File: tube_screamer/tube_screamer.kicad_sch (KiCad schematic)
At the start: 67 parts, among them J1 Jack_6.35, J2 Jack_6.35, J6 Barrel_Jack_Switch, J7 Conn_01x01_Socket, J8 Conn_01x01_Socket, J9 top_panel_connector, P1 front_plate, P2 bottom_plate, Q1 MMBT5551, Q10 AO3401A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

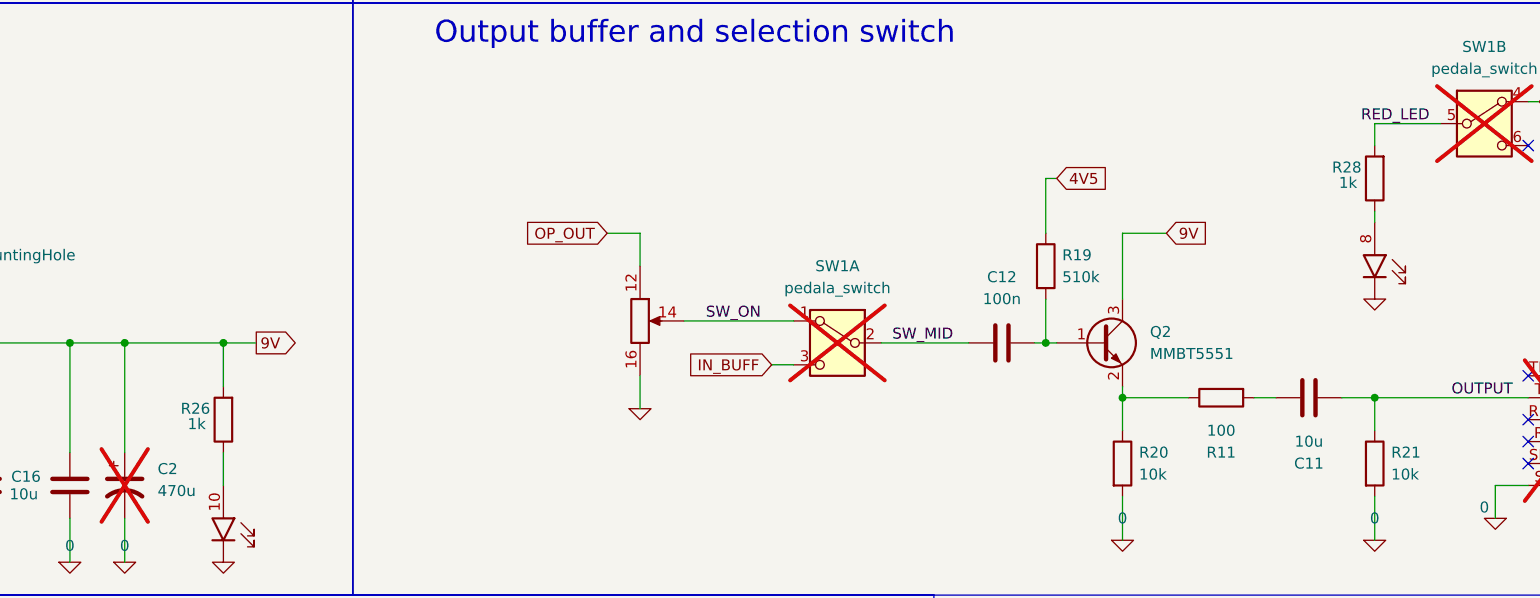
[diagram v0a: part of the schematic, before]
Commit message: 2.2 kOhm LED resistance.
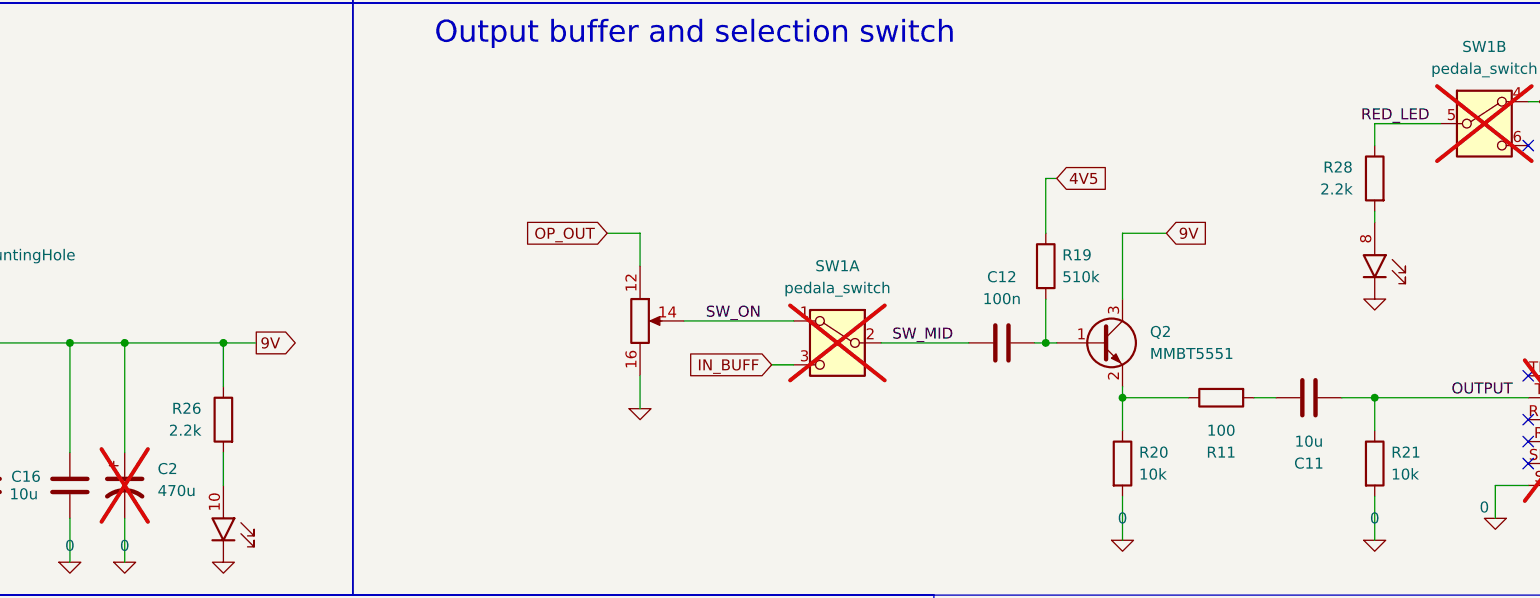
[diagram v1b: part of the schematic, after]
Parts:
- R26, R28: value 1k -> 2.2k; LCSC C21190 -> C4190
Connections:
- net 9V: now also R26.1; no longer R26.2
- net RED_LED: now also R28.1; no longer R28.2
- net at J9.8 (Pin_8): now also R28.2; no longer R28.1
- net at J9.10 (Pin_10): now also R26.2; no longer R26.1
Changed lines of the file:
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@@
 	)
 	(symbol
+		(lib_id "Device:R")
+		(at 93.98 128.27 0)
+		(mirror y)
+		(unit 1)
+		(exclude_from_sim no)
+		(in_bom yes)
+		(on_board yes)
+		(dnp no)
+		(property "Reference" "R26"
+			(at 91.44 126.9999 0)
+			(effects
+				(font
+					(size 1.27 1.27)
+				)
+				(justify left)
+			)
+		)
+		(property "Value" "2.2k"
+			(at 91.44 129.5399 0)
+			(effects
+				(font
+					(size 1.27 1.27)
+				)
+				(justify left)
+			)
+		)
+		(property "Footprint" "Resistor_SMD:R_0603_1608Metric_Pad0.98x0.95mm_HandSolder"
+			(at 95.758 128.27 90)
+			(effects
+				(font
+					(size 1.27 1.27)
+				)
+				(hide yes)
+			)
+		)
+		(property "Datasheet" "~"
+			(at 93.98 128.27 0)
+			(effects
+				(font
+					(size 1.27 1.27)
+				)
+				(hide yes)
+			)
+		)
+		(property "Description" ""
+			(at 93.98 128.27 0)
+			(effects
+				(font
+					(size 1.27 1.27)
+				)
+			)
+		)
+		(property "LCSC" "C4190"
+			(at 93.98 128.27 90)
+			(effects
+				(font
+					(size 1.27 1.27)
+				)
+				(hide yes)
+			)
+		)
+		(pin "1"
+		)
+		(pin "2"
+		)
+		(instances
+			(project "tube_screamer"
+				(path "/e0801131-6974-42d8-8070-4ed960891aa7"
+					(reference "R26")
+					(unit 1)
+				)
+			)
+		)
+	)
+	(symbol
 		(lib_id "pedale:top_panel_connector")
 		(at 181.61 163.83 0)
@@
 	)
 	(symbol
-		(lib_id "Device:R")
-		(at 227.33 100.33 180)
-		(unit 1)
-		(exclude_from_sim no)
-		(in_bom yes)
-		(on_board yes)
-		(dnp no)
-		(property "Reference" "R28"
-			(at 225.806 99.06 0)
-			(effects
-				(font
-					(size 1.27 1.27)
-				)
-				(justify left)
-			)
-		)
-		(property "Value" "1k"
-			(at 225.298 100.838 0)
-			(effects
-				(font
-					(size 1.27 1.27)
-				)
-				(justify left)
-			)
-		)
-		(property "Footprint" "Resistor_SMD:R_0603_1608Metric_Pad0.98x0.95mm_HandSolder"
-			(at 229.108 100.33 90)
-			(effects
-				(font
-					(size 1.27 1.27)
-				)
-				(hide yes)
-			)
-		)
-		(property "Datasheet" "~"
-			(at 227.33 100.33 0)
-			(effects
-				(font
-					(size 1.27 1.27)
-				)
-				(hide yes)
-			)
-		)
-		(property "Description" ""
-			(at 227.33 100.33 0)
-			(effects
-				(font
-					(size 1.27 1.27)
-				)
-			)
-		)
-		(property "LCSC" "C21190"
-			(at 227.33 100.33 90)
-			(effects
-				(font
-					(size 1.27 1.27)
-				)
-				(hide yes)
-			)
-		)
-		(pin "1"
-		)
-		(pin "2"
-		)
-		(instances
-			(project "tube_screamer"
-				(path "/e0801131-6974-42d8-8070-4ed960891aa7"
-					(reference "R28")
-					(unit 1)
-				)
-			)
-		)
-	)
-	(symbol
 		(lib_name "0_10")
 		(lib_id "Simulation_SPICE:0")
@@
 	)
 	(symbol
+		(lib_id "Device:R")
+		(at 227.33 100.33 0)
+		(mirror y)
+		(unit 1)
+		(exclude_from_sim no)
+		(in_bom yes)
+		(on_board yes)
+		(dnp no)
+		(property "Reference" "R28"
+			(at 224.79 99.0599 0)
+			(effects
+				(font
+					(size 1.27 1.27)
+				)
+				(justify left)
+			)
+		)
+		(property "Value" "2.2k"
+			(at 224.79 101.5999 0)
+			(effects
+				(font
+					(size 1.27 1.27)
+				)
+				(justify left)
+			)
+		)
+		(property "Footprint" "Resistor_SMD:R_0603_1608Metric_Pad0.98x0.95mm_HandSolder"
+			(at 229.108 100.33 90)
+			(effects
+				(font
+					(size 1.27 1.27)
+				)
+				(hide yes)
+			)
+		)
+		(property "Datasheet" "~"
+			(at 227.33 100.33 0)
+			(effects
+				(font
+					(size 1.27 1.27)
+				)
+				(hide yes)
+			)
+		)
+		(property "Description" ""
+			(at 227.33 100.33 0)
+			(effects
+				(font
+					(size 1.27 1.27)
+				)
+			)
+		)
+		(property "LCSC" "C4190"
+			(at 227.33 100.33 90)
+			(effects
+				(font
+					(size 1.27 1.27)
+				)
+				(hide yes)
+			)
+		)
+		(pin "1"
+		)
+		(pin "2"
+		)
+		(instances
+			(project "tube_screamer"
+				(path "/e0801131-6974-42d8-8070-4ed960891aa7"
+					(reference "R28")
+					(unit 1)
+				)
+			)
+		)
+	)
+	(symbol
 		(lib_id "Transistor_FET:AO3400A")
 		(at 96.52 163.83 0)
@@
 					(unit 1)
 				)
-			)
-		)
-	)
-	(symbol
-		(lib_id "Device:R")
-		(at 93.98 128.27 180)
-		(unit 1)
-		(exclude_from_sim no)
-		(in_bom yes)
-		(on_board yes)
-		(dnp no)
-		(property "Reference" "R26"
-			(at 92.456 127 0)
-			(effects
-				(font
-					(size 1.27 1.27)
-				)
-				(justify left)
-			)
-		)
-		(property "Value" "1k"
-			(at 91.948 128.778 0)
-			(effects
-				(font
-					(size 1.27 1.27)
-				)
-				(justify left)
-			)
-		)
-		(property "Footprint" "Resistor_SMD:R_0603_1608Metric_Pad0.98x0.95mm_HandSolder"
-			(at 95.758 128.27 90)
-			(effects
-				(font
-					(size 1.27 1.27)
-				)
-				(hide yes)
-			)
-		)
-		(property "Datasheet" "~"
-			(at 93.98 128.27 0)
-			(effects
-				(font
-					(size 1.27 1.27)
-				)
-				(hide yes)
-			)
-		)
-		(property "Description" ""
-			(at 93.98 128.27 0)
-			(effects
-				(font
-					(size 1.27 1.27)
-				)
-			)
-		)
-		(property "LCSC" "C21190"
-			(at 93.98 128.27 90)
-			(effects
-				(font
-					(size 1.27 1.27)
-				)
-				(hide yes)
-			)
-		)
-		(pin "1"
-		)
-		(pin "2"
-		)
-		(instances
-			(project "tube_screamer"
-				(path "/e0801131-6974-42d8-8070-4ed960891aa7"
-					(reference "R26")
-					(unit 1)
-				)

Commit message: dafsd
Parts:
- J9: footprint Connector_IDC:IDC-Header_2x08_P2.54mm_Vertical -> pedale:IDC-Header_2x08_P2.54mm_Vertical
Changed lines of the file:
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@@
 			)
 		)
-		(property "Footprint" "Connector_IDC:IDC-Header_2x08_P2.54mm_Vertical"
+		(property "Footprint" "pedale:IDC-Header_2x08_P2.54mm_Vertical"
 			(at 181.61 163.83 0)
 			(effects
@@
 			)
 		)
-		(property "Footprint" "Connector_IDC:IDC-Header_2x08_P2.54mm_Vertical"
+		(property "Footprint" "pedale:IDC-Header_2x08_P2.54mm_Vertical"
 			(at 180.34 29.21 0)
 			(effects
@@
 			)
 		)
-		(property "Footprint" "Connector_IDC:IDC-Header_2x08_P2.54mm_Vertical"
+		(property "Footprint" "pedale:IDC-Header_2x08_P2.54mm_Vertical"
 			(at 93.98 140.97 0)
 			(effects
@@
 			)
 		)
-		(property "Footprint" "Connector_IDC:IDC-Header_2x08_P2.54mm_Vertical"
+		(property "Footprint" "pedale:IDC-Header_2x08_P2.54mm_Vertical"
 			(at 161.29 29.21 0)
 			(effects
@@
 			)
 		)
-		(property "Footprint" "Connector_IDC:IDC-Header_2x08_P2.54mm_Vertical"
+		(property "Footprint" "pedale:IDC-Header_2x08_P2.54mm_Vertical"
 			(at 142.24 116.84 0)
 			(effects
@@
 			)
 		)
-		(property "Footprint" "Connector_IDC:IDC-Header_2x08_P2.54mm_Vertical"
+		(property "Footprint" "pedale:IDC-Header_2x08_P2.54mm_Vertical"
 			(at 227.33 110.49 0)
 			(effects
@@
 			)
 		)
-		(property "Footprint" "Connector_IDC:IDC-Header_2x08_P2.54mm_Vertical"
+		(property "Footprint" "pedale:IDC-Header_2x08_P2.54mm_Vertical"
 			(at 215.9 161.29 0)
 			(effects

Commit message: Done.
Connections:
- net 9V: now also SW1.6 (C); no longer SW1.4 (A)
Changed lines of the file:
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@@
 		(lib_id "pedale:pedala_switch")
 		(at 240.03 93.98 0)
+		(mirror x)
 		(unit 2)
 		(exclude_from_sim no)
@@
 		(dnp yes)
 		(property "Reference" "SW1"
-			(at 240.03 85.09 0)
+			(at 240.03 102.87 0)
 			(effects
 				(font
@@
 		)
 		(property "Value" "pedala_switch"
-			(at 240.03 87.63 0)
+			(at 240.03 100.33 0)
 			(effects
 				(font

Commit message: Ready for production.
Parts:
- R7: LCSC C25804 -> C22962
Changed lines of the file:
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@@
 			)
 		)
-		(property "LCSC" "C25804"
+		(property "LCSC" "C22962"
 			(at 180.34 48.26 0)
 			(effects
